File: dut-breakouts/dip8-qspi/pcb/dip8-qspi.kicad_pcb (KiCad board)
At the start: 4 copper layers, 58.5 x 20.5 mm, 10 parts, among them J1 CONN_DUMPTRUCK_DEVICE, U1 M24C02-RMC6TG, U2 DUT_SOCKET

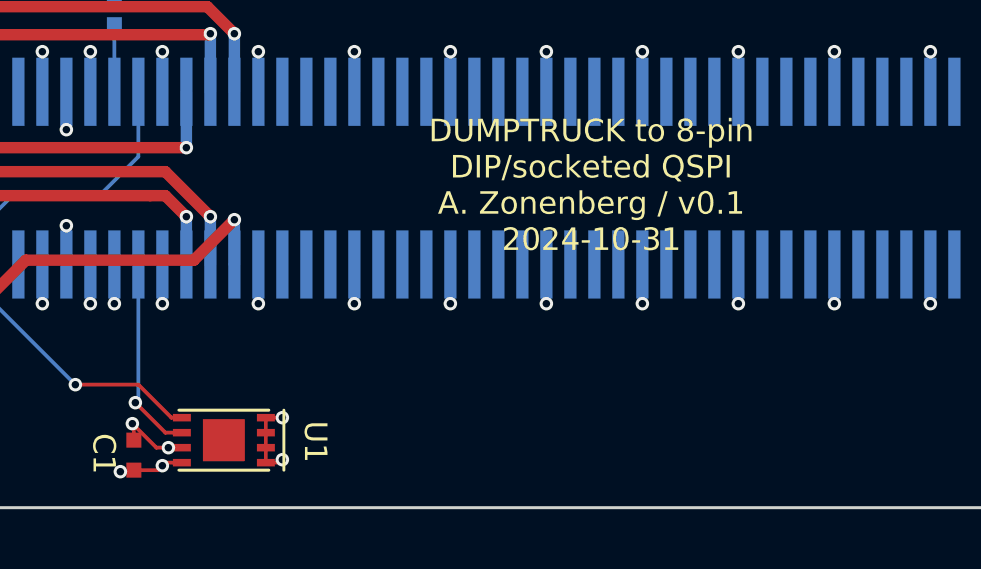
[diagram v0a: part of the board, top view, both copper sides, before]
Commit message: dip8-qspi: changed eeprom address to 0xa2
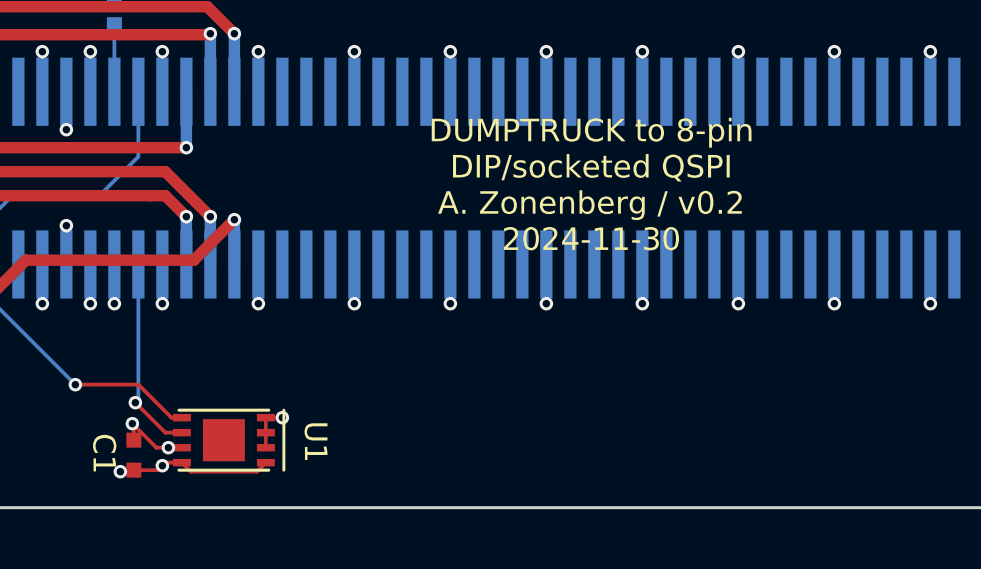
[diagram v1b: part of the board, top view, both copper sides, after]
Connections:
- U1 pad 1: /GND -> /3V3_EEPROM
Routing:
- net /3V3_EEPROM: track 22.1 -> 25.2 mm
- net /GND: track 144.2 -> 141.7 mm, vias 28 -> 27
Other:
- board text added: "DUMPTRUCK to 8-pin DIP/socketed QSPI A. Zonenberg / v0.2 2024-11-30"
- board text removed: "DUMPTRUCK to 8-pin DIP/socketed QSPI A. Zonenberg / v0.1 2024-10-31"
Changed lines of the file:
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@@
 		)
 		(property "Value" "M24C02-RMC6TG"
-			(at -3.75 -1.1 270)
+			(at -3.75 -1.1 -90)
 			(layer "F.SilkS")
 			(hide yes)
@@
 			(size 0.25 0.6)
 			(layers "F.Cu" "F.Paste" "F.Mask")
-			(net 2 "/GND")
+			(net 1 "/3V3_EEPROM")
 			(pinfunction "A0")
 			(pintype "input")
@@
 		)
 		(property "Value" "0.47 uF"
-			(at 0.05 3.1 270)
+			(at 0.05 3.1 -90)
 			(layer "F.SilkS")
 			(hide yes)
@@
 		)
 		(property "Value" "4.7 uF"
-			(at 0 3 270)
+			(at 0 3 -90)
 			(layer "F.SilkS")
 			(hide yes)
@@
 		)
 		(property "Value" "0.47 uF"
-			(at 0.05 3.1 270)
+			(at 0.05 3.1 -90)
 			(layer "F.SilkS")
 			(hide yes)
@@
 		)
 		(property "Value" "10K"
-			(at 0 3.5 270)
+			(at 0 3.5 -90)
 			(layer "F.SilkS")
 			(hide yes)
@@
 		(layer "Edge.Cuts")
 	)
-	(gr_text "DUMPTRUCK to 8-pin\nDIP/socketed QSPI\nA. Zonenberg / v0.1\n2024-10-31"
+	(gr_text "DUMPTRUCK to 8-pin\nDIP/socketed QSPI\nA. Zonenberg / v0.2\n2024-11-30"
 		(at 70.5 37.5 0)
 		(layer "F.SilkS")
@@
 	)
 	(segment
+		(start 56.85 44.500001)
+		(end 57.149999 44.8)
+		(width 0.125)
+		(layer "F.Cu")
+		(net 1)
+	)
+	(segment
 		(start 56.050001 44.749999)
 		(end 56.2 44.6)
@@
 		(net 1)
 	)
+	(segment
+		(start 59.350001 44.8)
+		(end 59.65 44.500001)
+		(width 0.125)
+		(layer "F.Cu")
+		(net 1)
+	)
+	(segment
+		(start 57.149999 44.8)
+		(end 59.350001 44.8)
+		(width 0.125)
+		(layer "F.Cu")
+		(net 1)
+	)
 	(via
 		(at 54.8 44.8)
@@
 	)
 	(segment
-		(start 59.65 42.999999)
-		(end 59.65 44.500001)
-		(width 0.125)
-		(layer "F.Cu")
-		(net 2)
-	)
-	(segment
 		(start 55.25 43.25)
 		(end 55.2 43.2)
-		(width 0.125)
-		(layer "F.Cu")
-		(net 2)
-	)
-	(segment
-		(start 60.099999 44.500001)
-		(end 60.2 44.4)
 		(width 0.125)
 		(layer "F.Cu")
@@
 	)
 	(segment
-		(start 59.65 44.500001)
-		(end 60.099999 44.500001)
-		(width 0.125)
-		(layer "F.Cu")
-		(net 2)
-	)
-	(segment
 		(start 32.55 28.25)
 		(end 32.6 28.2)
@@
 	)
 	(segment
+		(start 59.65 44)
+		(end 59.65 42.999999)
+		(width 0.125)
+		(layer "F.Cu")
+		(net 2)
+	)
+	(segment
 		(start 39.75 40.75)
 		(end 40.35 40.75)
@@
 	)
 	(via
-		(at 60.2 44.4)
-		(size 0.45)
-		(drill 0.25)
-		(layers "F.Cu" "B.Cu")
-		(net 2)
-	)
-	(via
 		(at 32.6 28.2)
 		(size 0.45)
@@
 		(width 0.125)
 		(layer "In1.Cu")
-		(net 2)
-	)
-	(segment
-		(start 60.2 44.4)
-		(end 60.2 43)
-		(width 0.125)
-		(layer "In1.Cu")
